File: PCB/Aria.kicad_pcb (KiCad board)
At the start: 2 copper layers, 78 parts, among them J1 B2B-PH-K-S(LF)(SN), J2 B3B-PH-K-S(LF)(SN), J3 20021121-00010C4LF, J4 0475890001-MicroUSBPort, P1 CONN_01X20, P2 CONN_01X20, Q1 DMG2307L-7, Q2 DMG2307L-7, SW1 B3U-1000P, SW2 B3U-1000P, T1 1909763-1, U1 BQ24210DQCT, U2 AZ1117CR-3.3TRG1_1, U3 STM32F446RET6_-_TQFP64, U4 ESP8285, X1 ABM3B8.000MHZB2T, X2 ABS07-32.768KHZ-9-T, X3 FA-128_26.0000MF10Z-AC3

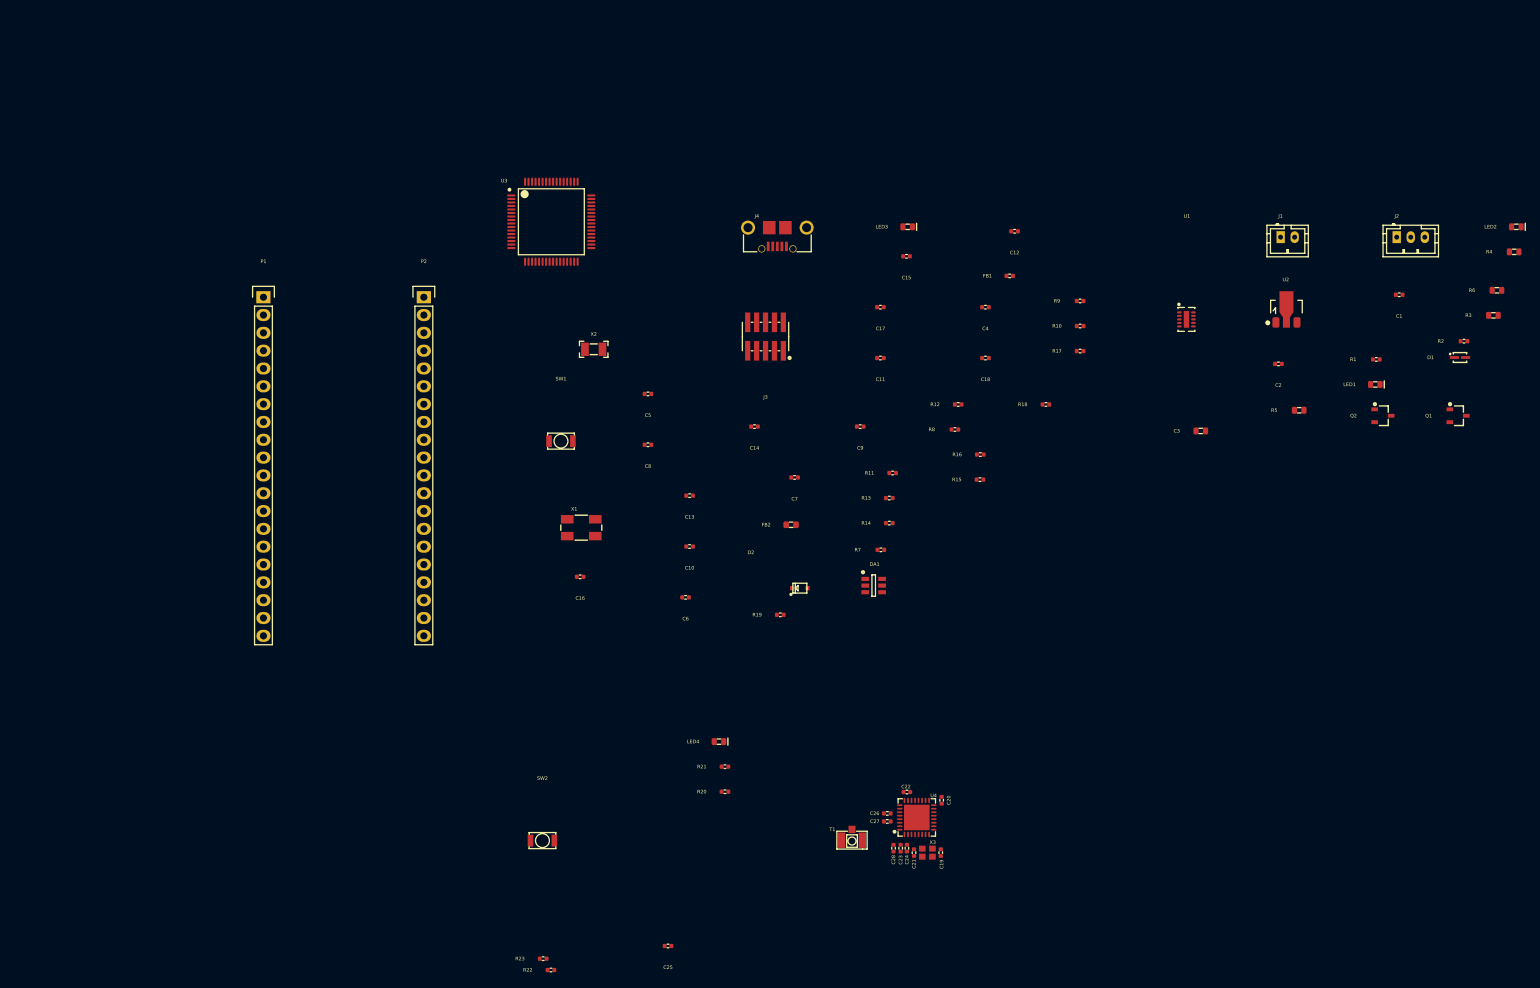
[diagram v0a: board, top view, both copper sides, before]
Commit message: Board Layout
Board layout started. ESP8285 component placement preliminary complete.
3D parts added and updated for ESP8285. STM32 and SOT32 3/6 pin
packages.
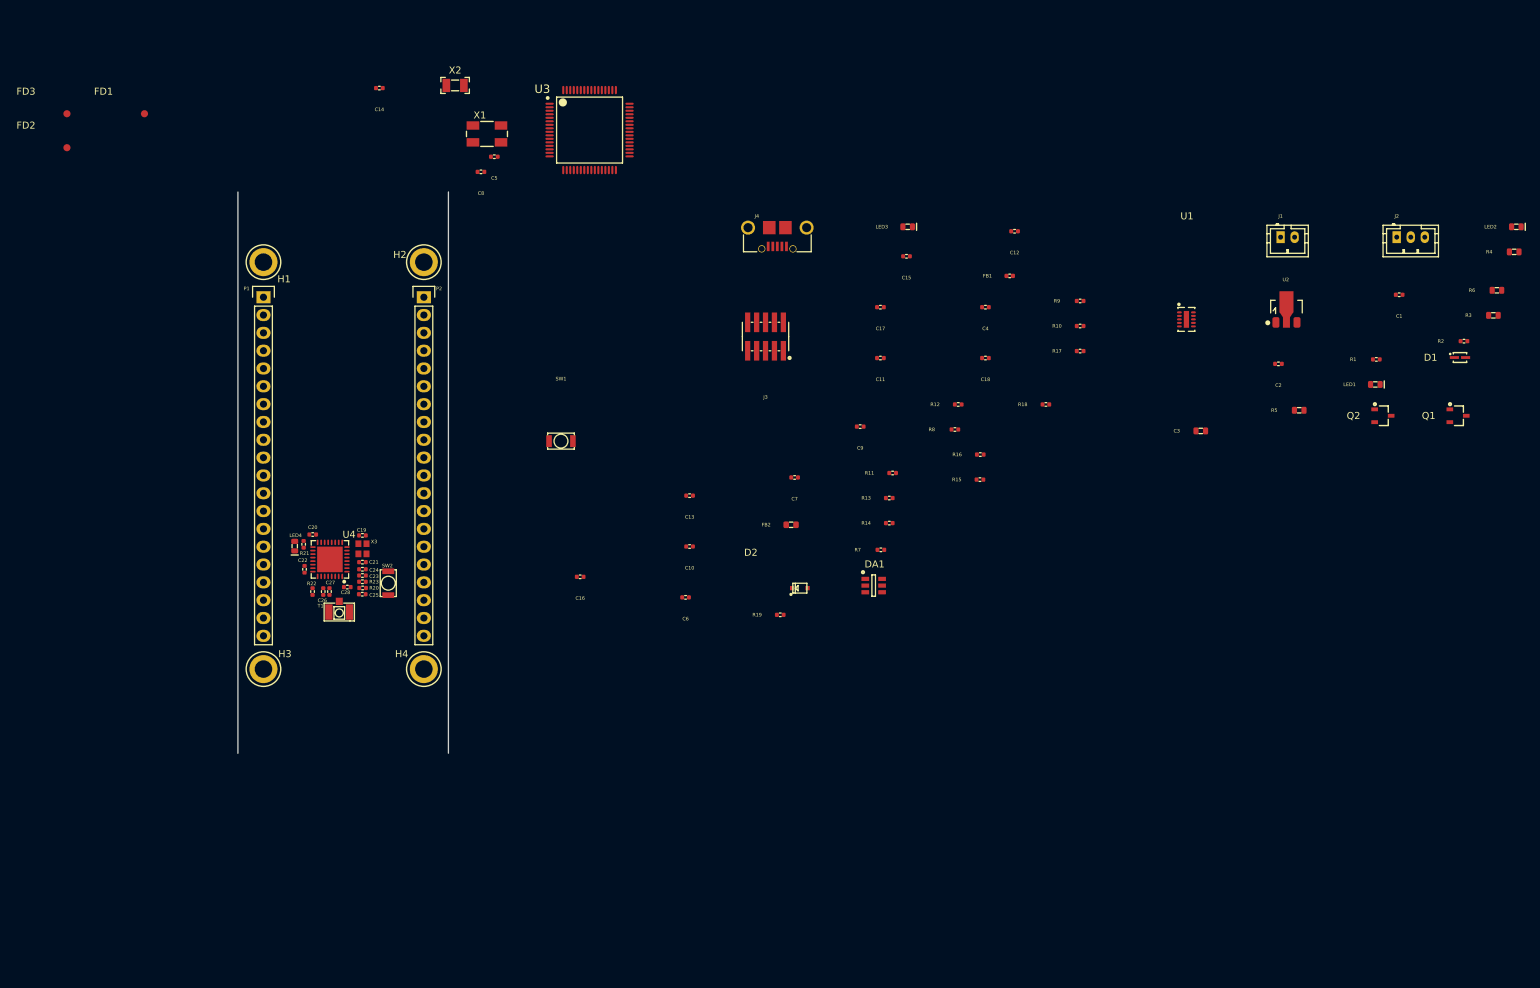
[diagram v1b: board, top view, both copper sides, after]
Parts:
- added FD1: FIDUCIAL, PCB_Footprints:FIDUCIAL, F.Cu at (40.2, 23.8)
- added FD2: FIDUCIAL, PCB_Footprints:FIDUCIAL, F.Cu at (29.1, 28.7)
- added FD3: FIDUCIAL, PCB_Footprints:FIDUCIAL, F.Cu at (29.1, 23.8)
- added H1: M2.5_Hole, PCB_Footprints:M2.5_HOLE, F.Cu at (57.1, 45.0)
- added H2: M2.5_Hole, PCB_Footprints:M2.5_HOLE, F.Cu at (80.0, 45.0)
- added H3: M2.5_Hole, PCB_Footprints:M2.5_HOLE, F.Cu at (57.1, 103.0)
- added H4: M2.5_Hole, PCB_Footprints:M2.5_HOLE, F.Cu at (80.0, 103.0)
- moved C20 97.3 mm to (64.2, 83.8), turned to 180 degrees
- moved C19 94.0 mm to (71.2, 83.9), turned to 0 degrees
- moved C22 91.5 mm to (63.0, 88.8), turned to 270 degrees
- moved X3 91.4 mm to (71.2, 85.9), turned to 270 degrees
- moved U4 91.4 mm to (66.6, 87.4), turned to 90 degrees
- moved C21 88.8 mm to (71.2, 87.8), turned to 180 degrees
- moved C24 87.2 mm to (71.2, 88.8), turned to 0 degrees
- moved C26 86.4 mm to (65.7, 91.9), turned to 270 degrees
- moved C28 86.3 mm to (69.1, 91.3), turned to 0 degrees
- moved C23 86.0 mm to (71.2, 89.7), turned to 0 degrees
- moved C27 86.0 mm to (66.5, 91.9), turned to 270 degrees
- moved T1 80.0 mm to (67.9, 94.9)
- moved C14 72.0 mm to (73.7, 20.2)
- moved R21 67.9 mm to (62.9, 85.2), turned to 270 degrees
- moved LED4 66.6 mm to (61.6, 85.5), turned to 270 degrees
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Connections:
- LED4 pad 2: Net-(LED4-Pad2) -> GND
- R21 pad 1: GND -> Net-(LED4-Pad1)
- R21 pad 2: Net-(LED4-Pad2) -> Net-(R21-Pad2)
- U4 pad 16: Net-(LED4-Pad1) -> Net-(R21-Pad2)
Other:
- board outline added: 30 x 80 mm

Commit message: Preliminary Formfactor
Preliminary formfactor designed. component placelement still underway
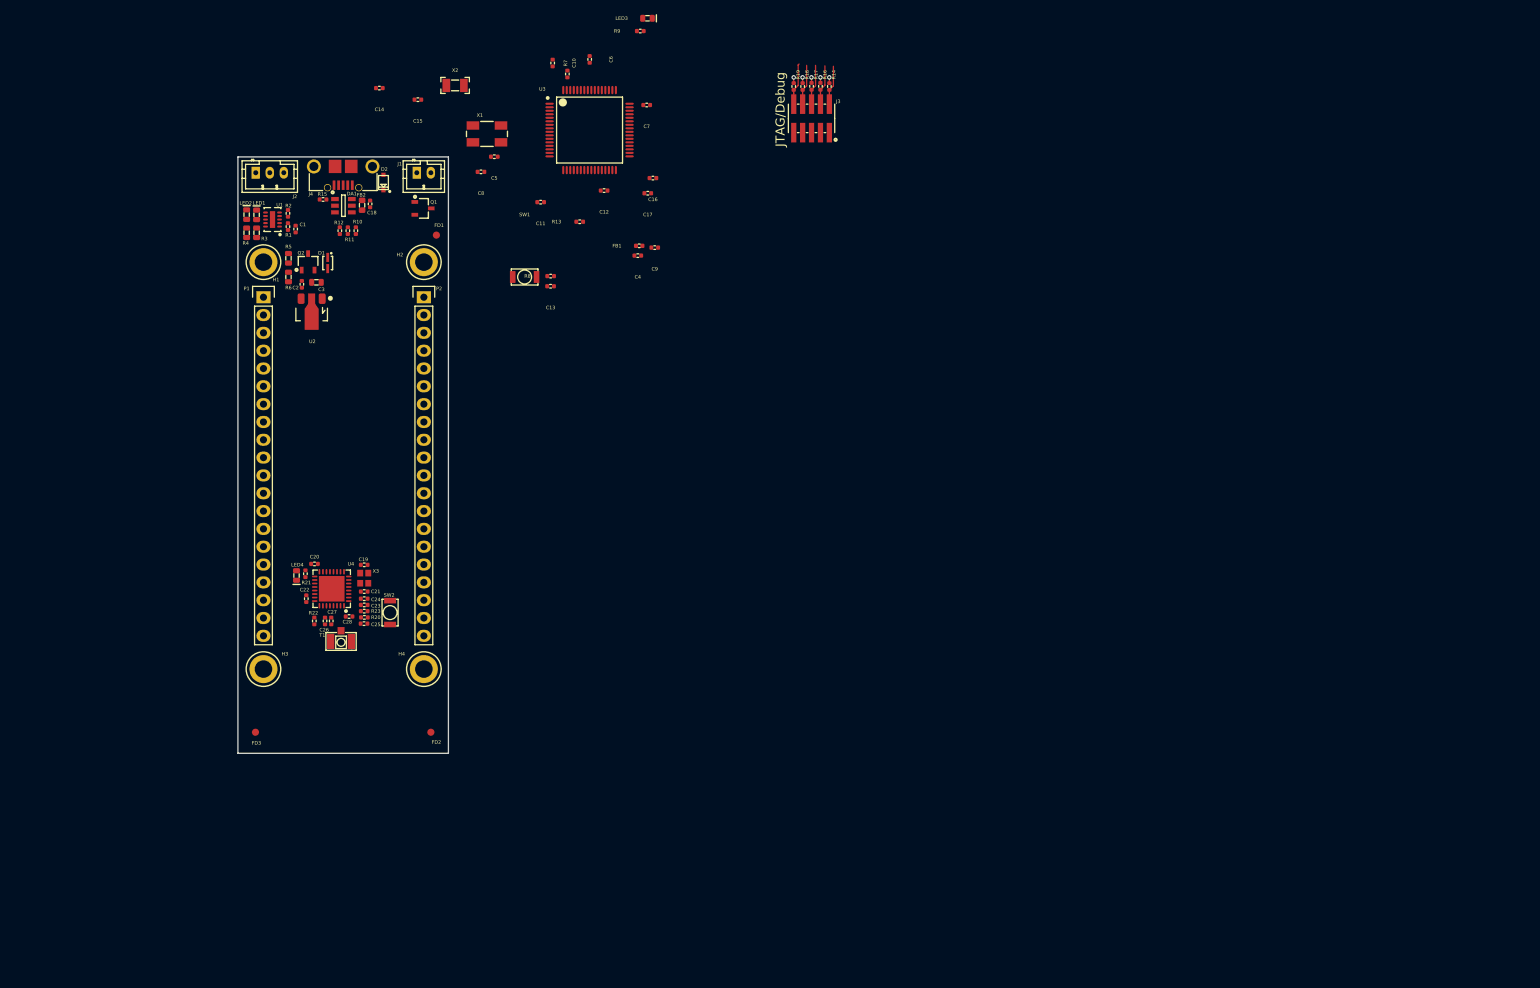
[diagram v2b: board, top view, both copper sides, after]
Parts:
- moved LED2 181.0 mm to (54.7, 38.2), turned to 90 degrees
- moved R4 180.7 mm to (54.7, 40.8), turned to 270 degrees
- moved R3 176.7 mm to (56.2, 40.8), turned to 270 degrees
- moved R6 172.2 mm to (60.7, 47.1), turned to 270 degrees
- moved R2 168.6 mm to (60.6, 38.0), turned to 90 degrees
- moved J2 162.9 mm to (56.0, 32.3)
- moved D1 161.9 mm to (66.3, 45.1), turned to 270 degrees
- moved LED1 161.3 mm to (56.2, 38.3), turned to 90 degrees
- moved C1 157.6 mm to (61.7, 40.3), turned to 90 degrees
- moved R1 156.3 mm to (60.6, 39.9), turned to 90 degrees
- moved Q2 154.8 mm to (63.5, 45.0), turned to 90 degrees
- moved Q1 150.4 mm to (79.9, 37.3)
- moved R5 145.7 mm to (60.7, 44.5), turned to 270 degrees
- moved C2 139.6 mm to (62.6, 48.2), turned to 90 degrees
- moved U2 138.9 mm to (64.0, 52.1), turned to 180 degrees
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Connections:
- P1 pad 1: Net-(P1-Pad1) -> GND
- P1 pad 2: Net-(P1-Pad2) -> +3V3
- P1 pad 20: Net-(P1-Pad20) -> GND
- P2 pad 1: Net-(P2-Pad1) -> GND
- P2 pad 2: Net-(P2-Pad2) -> +3V3
- P2 pad 20: Net-(P2-Pad20) -> GND
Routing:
- net /MCU_STM32F446RET6/NJTRST: track 0.00 -> 6.03 mm
- net /MCU_STM32F446RET6/SWO_TDO: track 0.00 -> 5.76 mm
- net /MCU_STM32F446RET6/SWO_TDI: track 0.00 -> 5.76 mm
- net /MCU_STM32F446RET6/SWCLK_TCK: track 0.00 -> 5.73 mm
- net /MCU_STM32F446RET6/SWDIO_TMS: track 0.00 -> 5.64 mm
- net +3V3: track 0.00 -> 4.03 mm, vias 0 -> 5
- added copper zone on In2.Cu, net +3V3
- added copper zone on In1.Cu, net GND
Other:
- board size 30 x 80 mm -> 30 x 85 mm
- copper layers 2 -> 4
- net class Default: clearance 0.2 -> 0.1778; trace_width 0.25 -> 0.1778; via_dia 0.8 -> 0.635; via_drill 0.4 -> 0.3302
- rule trace_clearance: 0.2 -> 0.1778
- rule trace_min: 0.2 -> 0.1778
- rule via_min_drill: 0.3 -> 0.3302
- rule via_min_size: 0.4 -> 0.635
- board text added: "JTAG/Debug"
